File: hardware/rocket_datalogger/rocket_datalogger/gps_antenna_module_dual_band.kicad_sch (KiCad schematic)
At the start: 1 part

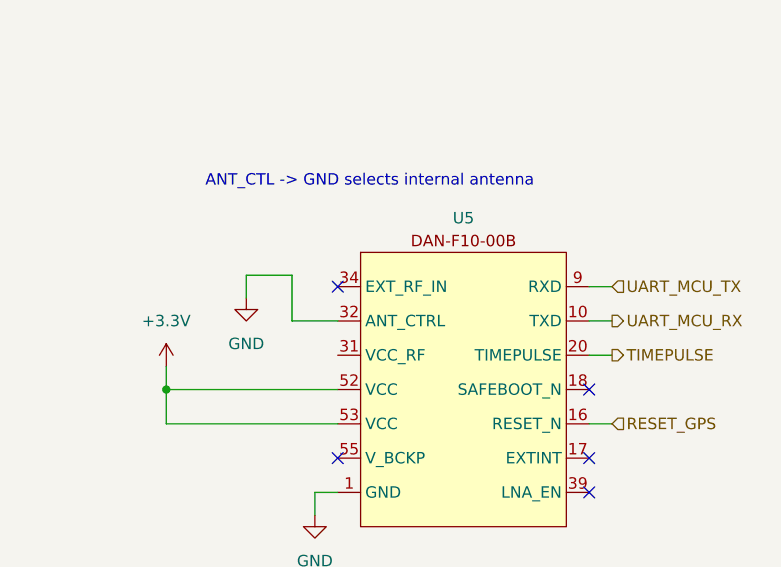
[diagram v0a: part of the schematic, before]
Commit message: Changed IMU to BNO055
Previous IMU required 1.85V rail
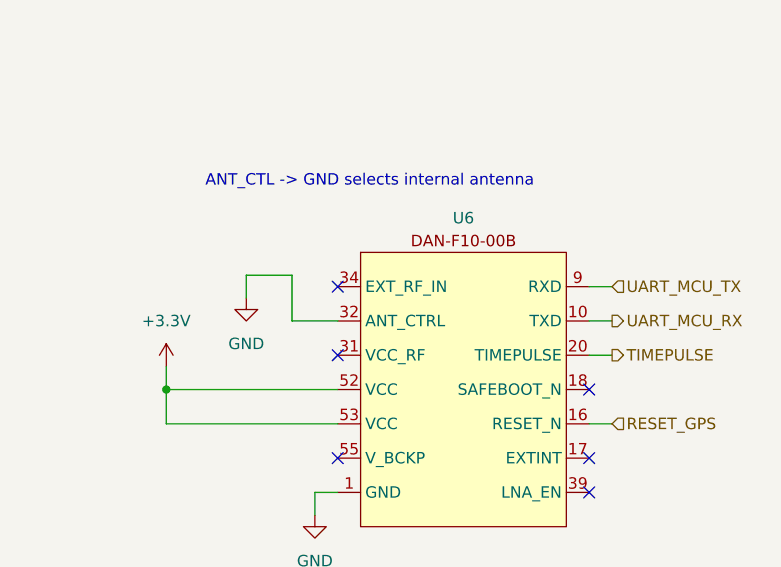
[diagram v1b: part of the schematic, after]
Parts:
- renumbered U5 to U6
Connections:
- no-connect marks 5 -> 6
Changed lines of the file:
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@@
+	)
+	(no_connect
+		(at 134.62 92.71)
 	)
 	(no_connect
@@
 		(dnp no)
 		(fields_autoplaced yes)
-		(property "Reference" "#PWR037"
+		(property "Reference" "#PWR051"
 			(at 124.46 92.71 0)
 			(effects
@@
 			(project ""
 				(path "/742f64ac-c4d8-4561-a2a9-e0e3f6f67ce8/f8f37d10-87ba-4177-9a91-b9e4738edda4"
-					(reference "#PWR037")
+					(reference "#PWR051")
 					(unit 1)
 				)
@@
 		(dnp no)
 		(fields_autoplaced yes)
-		(property "Reference" "#PWR038"
+		(property "Reference" "#PWR050"
 			(at 115.57 97.79 0)
 			(effects
@@
 			(project ""
 				(path "/742f64ac-c4d8-4561-a2a9-e0e3f6f67ce8/f8f37d10-87ba-4177-9a91-b9e4738edda4"
-					(reference "#PWR038")
+					(reference "#PWR050")
 					(unit 1)
 				)
@@
 		(dnp no)
 		(fields_autoplaced yes)
-		(property "Reference" "U5"
+		(property "Reference" "U6"
 			(at 148.59 77.47 0)
 			(effects
@@
 			(project ""
 				(path "/742f64ac-c4d8-4561-a2a9-e0e3f6f67ce8/f8f37d10-87ba-4177-9a91-b9e4738edda4"
-					(reference "U5")
+					(reference "U6")
 					(unit 1)
 				)
@@
 		(dnp no)
 		(fields_autoplaced yes)
-		(property "Reference" "#PWR036"
+		(property "Reference" "#PWR052"
 			(at 132.08 116.84 0)
 			(effects
@@
 			(project ""
 				(path "/742f64ac-c4d8-4561-a2a9-e0e3f6f67ce8/f8f37d10-87ba-4177-9a91-b9e4738edda4"
-					(reference "#PWR036")
+					(reference "#PWR052")
 					(unit 1)
 				)

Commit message: Minor revision
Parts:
- U6: footprint (none) -> rocket_datalogger:DAN-F10-00B
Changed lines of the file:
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@@
 			)
 		)
-		(property "Footprint" ""
+		(property "Footprint" "rocket_datalogger:DAN-F10-00B"
 			(at 148.59 95.25 0)
 			(effects

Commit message: PCB design rev 1
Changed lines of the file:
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@@
 		(pin "46"
+		)
+		(pin "EP1"
 		)
 		(instances
